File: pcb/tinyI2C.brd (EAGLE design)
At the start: 83.2 x 83.2 mm, 34 parts, among them IC1 74LVC1G125DCK, IC2 74LVC1G125DCK, IC3 IC_LDO_MIC5355, U1 LPC824M201JHI33, X1 TSW-112-02-S-S, X2 TSW-112-02-S-S, X3 TSW-106-02-S-S-RA, X4 TSW-102-02-S-S, X5 TSW-102-02-S-S, X6 TSW-102-02-S-S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

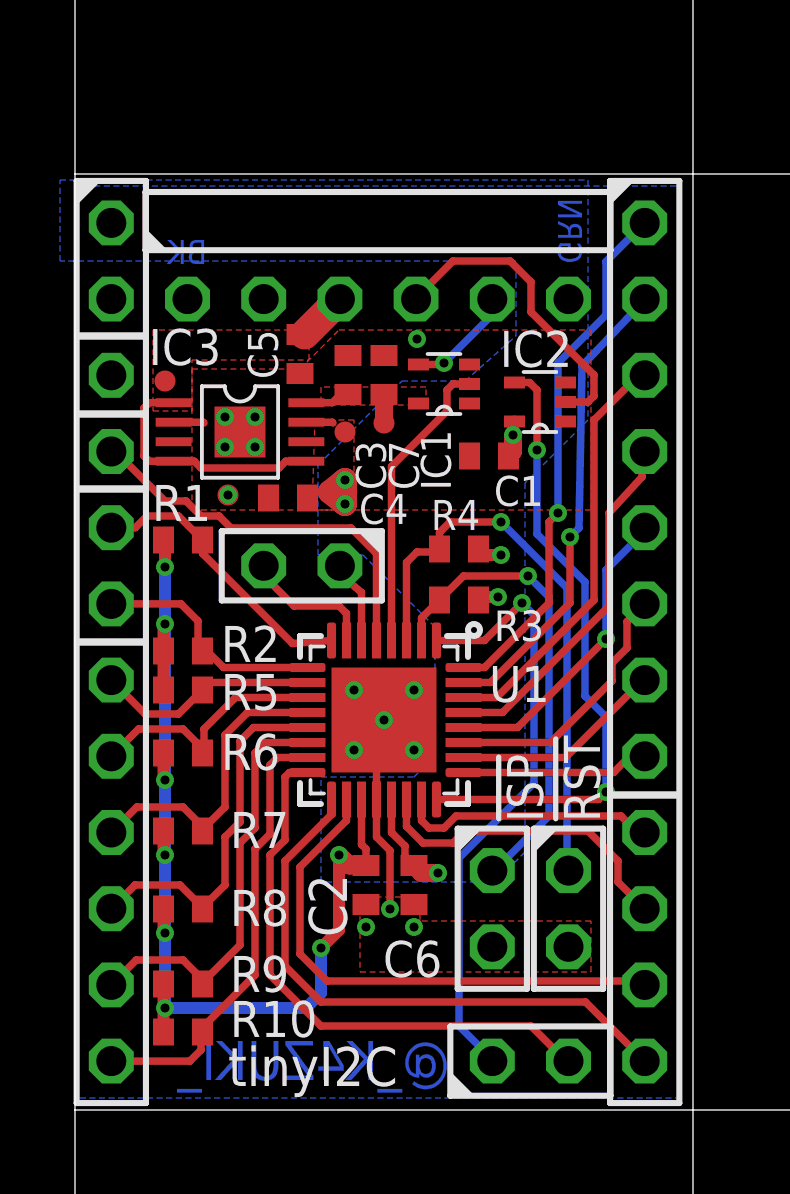
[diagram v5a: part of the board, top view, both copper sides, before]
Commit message: [ PCB ][ SCH ] X1[3] is now Vin(5V) [ BRD ] related tracechange
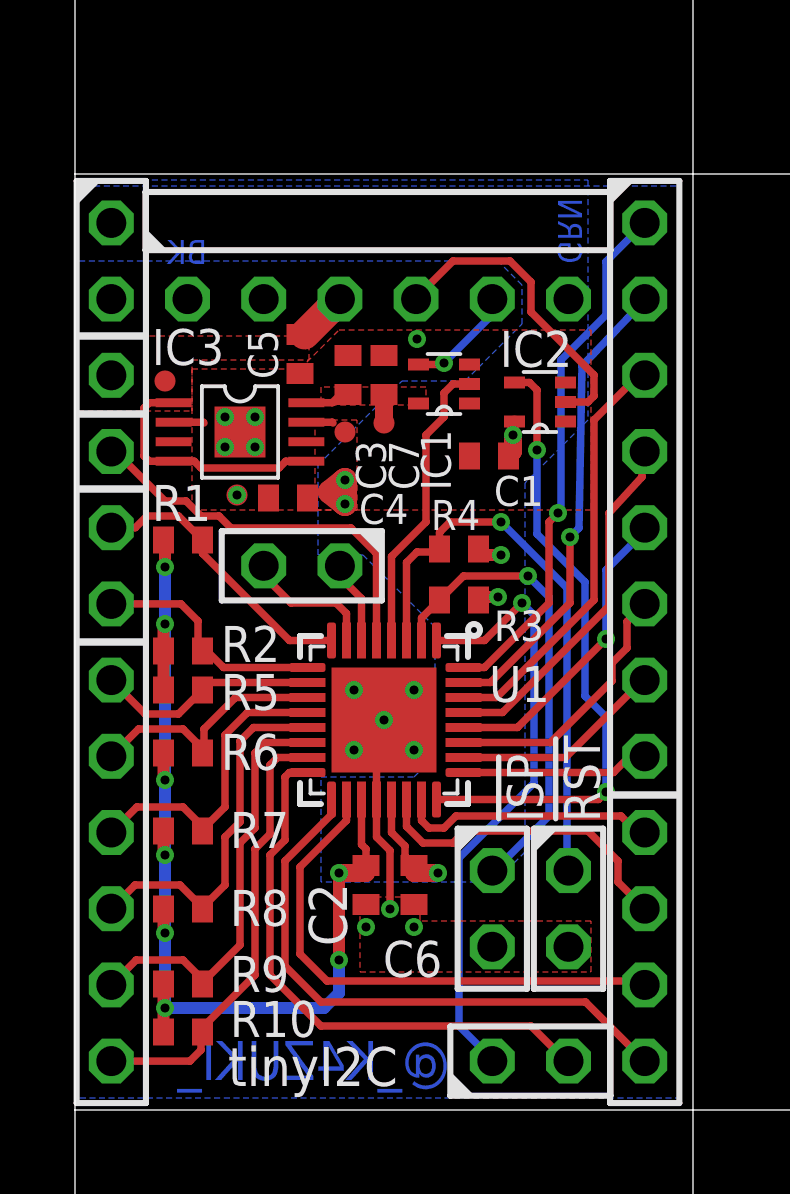
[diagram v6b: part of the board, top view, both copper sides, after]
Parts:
- moved TP3 0.30 mm to (5.40, 30.9)
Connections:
- net 5V: now also X1.3
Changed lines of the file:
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@@
 <text x="17.5" y="20" size="1.2" layer="21" font="vector" ratio="15" rot="R90">!RST</text>
 <text x="15.6" y="20" size="1.2" layer="21" font="vector" ratio="15" rot="R90">!ISP</text>
+<wire x1="6.8" y1="30.3" x2="6.8" y2="31.3" width="0.2" layer="41"/>
+<wire x1="6.8" y1="30.3" x2="6.1" y2="30.3" width="0.2" layer="41"/>
+<wire x1="6.8" y1="31.3" x2="6.1" y2="31.3" width="0.2" layer="41"/>
+<wire x1="0.2" y1="11" x2="0.2" y2="41" width="0.4" layer="41"/>
+<wire x1="20.1" y1="41" x2="0.2" y2="41" width="0.4" layer="41"/>
+<wire x1="20.1" y1="41" x2="20.1" y2="11" width="0.4" layer="41"/>
+<wire x1="0.2" y1="11" x2="20.1" y2="11" width="0.4" layer="41"/>
 </plain>
 <attributes>
@@
 </element>
 <element name="C2" library="mylib" package="C0402" value="1005" x="9.7" y="17.9" smashed="yes" rot="R270">
-<attribute name="NAME" x="9.065" y="16.165" size="1.27" layer="25" font="vector" ratio="15" rot="R90"/>
+<attribute name="NAME" x="9.065" y="15.865" size="1.27" layer="25" font="vector" ratio="15" rot="R90"/>
 <attribute name="VALUE" x="7.795" y="18.535" size="1.27" layer="27" rot="R270"/>
 </element>
@@
 <attribute name="VALUE" x="8.746" y="32.492" size="0.0254" layer="27"/>
 </element>
-<element name="TP3" library="testpad" package="TP07R" value="TPTP07R" x="5.1" y="30.9" smashed="yes">
-<attribute name="TP_SIGNAL_NAME" value="" x="5.1" y="28.995" size="1" layer="37"/>
-<attribute name="VALUE" x="4.846" y="30.392" size="0.0254" layer="27"/>
+<element name="TP3" library="testpad" package="TP07R" value="TPTP07R" x="5.4" y="30.9" smashed="yes">
+<attribute name="TP_SIGNAL_NAME" value="" x="5.4" y="28.995" size="1" layer="37"/>
+<attribute name="VALUE" x="5.146" y="30.392" size="0.0254" layer="27"/>
 </element>
 <element name="R1" library="mylib" package="C0402" value="220/1005" x="3.6" y="29.4" smashed="yes" rot="R180">
@@
 </element>
 <element name="IC3" library="mylib" package="IC_08_0.65_160MIL" value="IC_LDO_MIC5355" x="5.5" y="33" smashed="yes" rot="R270">
-<attribute name="NAME" x="2.46" y="35.232" size="1.2" layer="25" font="vector" ratio="15"/>
+<attribute name="NAME" x="2.56" y="35.232" size="1.2" layer="25" font="vector" ratio="15"/>
 <attribute name="VALUE" x="2.96" y="29.698" size="1.27" layer="27" ratio="10"/>
 </element>
@@
 </polygon>
 <via x="5" y="32.5" extent="1-16" drill="0.3"/>
-<via x="5.1" y="30.9" extent="1-16" drill="0.3"/>
+<via x="5.4" y="30.9" extent="1-16" drill="0.3"/>
 <via x="6" y="32.5" extent="1-16" drill="0.3"/>
 <polygon width="0.25" layer="1" thermals="no" rank="2">
@@
 <wire x1="6.8" y1="31.8" x2="4.2" y2="31.8" width="0.25" layer="1"/>
 <polygon width="0.25" layer="1" thermals="no" rank="3">
-<vertex x="2.6" y="33.7"/>
+<vertex x="0.1" y="33.7"/>
 <vertex x="3.9" y="33.7"/>
 <vertex x="3.9" y="35.4"/>
 <vertex x="7.8" y="35.4"/>
-<vertex x="7.8" y="36.4"/>
-<vertex x="2.6" y="36.4"/>
+<vertex x="7.8" y="36.2"/>
+<vertex x="0.1" y="36.2"/>
 </polygon>
 <wire x1="7.65" y1="36.25" x2="8.83" y2="37.43" width="1" layer="1"/>
@@
 <contactref element="IC3" pad="4"/>
 <contactref element="IC3" pad="5"/>
+<contactref element="X1" pad="3"/>
+<wire x1="7.5" y1="36.25" x2="7.65" y2="36.25" width="0.4" layer="1"/>
 </signal>
 <signal name="TX-&gt;">
@@
 <vertex x="10.9" y="34.7"/>
 <vertex x="13" y="34.7"/>
-<vertex x="14.7" y="36.2"/>
-<vertex x="14.7" y="38.7"/>
-<vertex x="-0.5" y="38.7"/>
-<vertex x="-0.5" y="41.4"/>
+<vertex x="14.9" y="36.6"/>
+<vertex x="14.9" y="37.9"/>
+<vertex x="14.1" y="38.7"/>
+<vertex x="0" y="38.7"/>
+<vertex x="0" y="41.4"/>
 <vertex x="17.1" y="41.4"/>
 <vertex x="17.1" y="33.4"/>
@@
 <contactref element="C6" pad="1"/>
 <wire x1="10.55" y1="19.65" x2="11" y2="19.2" width="0.25" layer="1"/>
-<via x="8.8" y="18.9" extent="1-16" drill="0.3"/>
+<via x="8.8" y="18.3" extent="1-16" drill="0.3"/>
 <wire x1="11" y1="19.2" x2="11" y2="18.85" width="0.25" layer="1"/>
-<wire x1="12.1" y1="18.3" x2="11.55" y2="18.3" width="0.6" layer="1"/>
+<wire x1="12.1" y1="18.3" x2="11.3" y2="18.3" width="0.6" layer="1"/>
 <wire x1="3" y1="18.9" x2="3" y2="21.4" width="0.4" layer="16"/>
 <wire x1="3" y1="16.3" x2="3" y2="18.9" width="0.4" layer="16"/>
 <wire x1="3" y1="13.8" x2="3" y2="16.3" width="0.4" layer="16"/>
-<via x="8.2" y="15.8" extent="1-16" drill="0.3" diameter="0.6"/>
+<via x="8.8" y="15.4" extent="1-16" drill="0.3" diameter="0.6"/>
 <wire x1="11" y1="18.85" x2="11.3" y2="18.55" width="0.25" layer="1"/>
-<wire x1="11.55" y1="18.3" x2="11.3" y2="18.55" width="0.6" layer="1"/>
-<wire x1="9.7" y1="18.55" x2="9.15" y2="18.55" width="0.6" layer="1"/>
-<wire x1="9.15" y1="18.55" x2="8.8" y2="18.9" width="0.6" layer="1"/>
 <wire x1="9.55" y1="20.75" x2="9.55" y2="19.25" width="0.25" layer="1"/>
 <wire x1="9.7" y1="18.55" x2="9.7" y2="19.1" width="0.25" layer="1"/>
@@
 <wire x1="2.95" y1="13" x2="2.95" y2="13.75" width="0.4" layer="1"/>
 <wire x1="2.95" y1="13.75" x2="3" y2="13.8" width="0.4" layer="1"/>
-<wire x1="8.8" y1="18.9" x2="8.8" y2="16.4" width="0.4" layer="1"/>
-<wire x1="8.2" y1="15.8" x2="8.2" y2="14.3" width="0.4" layer="16"/>
-<wire x1="8.2" y1="15.8" x2="8.8" y2="16.4" width="0.4" layer="1"/>
-<wire x1="3" y1="13.8" x2="7.7" y2="13.8" width="0.4" layer="16"/>
-<wire x1="7.7" y1="13.8" x2="8.2" y2="14.3" width="0.4" layer="16"/>
+<wire x1="8.8" y1="18.3" x2="8.8" y2="15.4" width="0.4" layer="1"/>
+<wire x1="8.8" y1="15.4" x2="8.8" y2="14.3" width="0.4" layer="16"/>
+<wire x1="3" y1="13.8" x2="8.3" y2="13.8" width="0.4" layer="16"/>
+<wire x1="8.3" y1="13.8" x2="8.8" y2="14.3" width="0.4" layer="16"/>
 <wire x1="7.712" y1="33.326" x2="8.574" y2="33.326" width="0.25" layer="1"/>
 <wire x1="8.574" y1="33.326" x2="8.6" y2="33.3" width="0.25" layer="1"/>
 <contactref element="IC2" pad="5"/>
 <polygon width="0.25" layer="1" thermals="no">
-<vertex x="9.3" y="33.4"/>
+<vertex x="9.4" y="33.4"/>
 <vertex x="8" y="33.4"/>
-<vertex x="7.9" y="30.4"/>
-<vertex x="9.3" y="30.4"/>
+<vertex x="8" y="30.4"/>
+<vertex x="9.4" y="30.4"/>
 </polygon>
 <contactref element="IC3" pad="7"/>
@@
 <wire x1="14.6" y1="32.9" x2="14.6" y2="32.35" width="0.6" layer="1"/>
 <wire x1="14.6" y1="32.35" x2="14.45" y2="32.2" width="0.6" layer="1"/>
+<wire x1="8.8" y1="18.3" x2="9.7" y2="18.3" width="0.6" layer="1"/>
+<wire x1="9.7" y1="18.3" x2="9.7" y2="18.55" width="0.6" layer="1"/>
+<wire x1="11.3" y1="18.3" x2="11.3" y2="18.55" width="0.6" layer="1"/>
 </signal>
 <signal name="TGT_TX">
 <contactref element="U1" pad="4"/>
-<wire x1="10.55" y1="26.05" x2="10.55" y2="31.85" width="0.25" layer="1"/>
+<wire x1="10.55" y1="26.05" x2="10.55" y2="28.85" width="0.25" layer="1"/>
 <contactref element="IC1" pad="2"/>
-<wire x1="10.55" y1="31.85" x2="12.4" y2="33.7" width="0.25" layer="1"/>
+<wire x1="10.55" y1="28.85" x2="11.7" y2="30" width="0.25" layer="1"/>
 <wire x1="13.15" y1="34.6" x2="12.6" y2="34.6" width="0.25" layer="1"/>
-<wire x1="12.6" y1="34.6" x2="12.4" y2="34.4" width="0.25" layer="1"/>
-<wire x1="12.4" y1="34.4" x2="12.4" y2="33.7" width="0.25" layer="1"/>
+<wire x1="12.6" y1="34.6" x2="12.3" y2="34.3" width="0.25" layer="1"/>
+<wire x1="12.3" y1="34.3" x2="12.3" y2="33.5" width="0.25" layer="1"/>
+<wire x1="12.3" y1="33.5" x2="11.7" y2="32.9" width="0.25" layer="1"/>
+<wire x1="11.7" y1="32.9" x2="11.7" y2="30" width="0.25" layer="1"/>
 </signal>
 <signal name="TGT_RX">
@@
 <signal name="SWCLK">
 <contactref element="U1" pad="6"/>
-<wire x1="9.55" y1="26.05" x2="9.55" y2="27.65" width="0.25" layer="1"/>
+<wire x1="9.55" y1="26.05" x2="9.55" y2="27.45" width="0.25" layer="1"/>
 <contactref element="X5" pad="1"/>
-<wire x1="8.83" y1="28.54" x2="8.83" y2="28.27" width="0.25" layer="1"/>
-<wire x1="8.83" y1="28.27" x2="9.55" y2="27.65" width="0.25" layer="1"/>
+<wire x1="8.83" y1="28.54" x2="8.83" y2="28.17" width="0.25" layer="1"/>
+<wire x1="8.83" y1="28.17" x2="9.55" y2="27.45" width="0.25" layer="1"/>
 </signal>
 <signal name="SWDIO">
 <contactref element="U1" pad="7"/>
 <wire x1="9.05" y1="26.05" x2="9.05" y2="26.95" width="0.25" layer="1"/>
-<wire x1="9.05" y1="26.95" x2="8.8" y2="27.2" width="0.25" layer="1"/>
-<wire x1="8.8" y1="27.2" x2="7.3" y2="27.2" width="0.25" layer="1"/>
+<wire x1="9.05" y1="26.95" x2="8.7" y2="27.3" width="0.25" layer="1"/>
+<wire x1="8.7" y1="27.3" x2="7.2" y2="27.3" width="0.25" layer="1"/>
 <contactref element="X5" pad="2"/>
-<wire x1="6.29" y1="28.21" x2="7.3" y2="27.2" width="0.25" layer="1"/>
+<wire x1="6.29" y1="28.21" x2="7.2" y2="27.3" width="0.25" layer="1"/>
 <wire x1="6.29" y1="28.54" x2="6.29" y2="28.21" width="0.25" layer="1"/>
 </signal>
@@
 <contactref element="R1" pad="1"/>
 <contactref element="X1" pad="5"/>
-<wire x1="8.55" y1="26.05" x2="7.25" y2="25.95" width="0.25" layer="1"/>
+<wire x1="8.55" y1="26.05" x2="7.15" y2="26.05" width="0.25" layer="1"/>
 <wire x1="1.21" y1="29.81" x2="2.01" y2="29.81" width="0.25" layer="1"/>
 <wire x1="2.01" y1="29.81" x2="2.4" y2="30.2" width="0.25" layer="1"/>
@@
 <wire x1="3.45" y1="30.2" x2="4.25" y2="29.4" width="0.25" layer="1"/>
 <wire x1="4.25" y1="29.4" x2="4.25" y2="28.95" width="0.25" layer="1"/>
-<wire x1="4.25" y1="28.95" x2="7.25" y2="25.95" width="0.25" layer="1"/>
+<wire x1="4.25" y1="28.95" x2="7.15" y2="26.05" width="0.25" layer="1"/>
 </signal>
 <signal name="I2C_SCL">
@@
 <wire x1="15.8" y1="27.3" x2="15.8" y2="30" width="0.25" layer="1"/>
 <wire x1="15.8" y1="30" x2="16.1" y2="30.3" width="0.25" layer="1"/>
-<wire x1="16.1" y1="30.3" x2="16.1" y2="35.3" width="0.25" layer="16"/>
-<wire x1="16.1" y1="35.3" x2="17.7" y2="36.9" width="0.25" layer="16"/>
+<wire x1="16.1" y1="30.3" x2="16.2" y2="30.4" width="0.25" layer="16"/>
+<wire x1="16.2" y1="30.4" x2="16.2" y2="35.4" width="0.25" layer="16"/>
+<wire x1="16.2" y1="35.4" x2="17.7" y2="36.9" width="0.25" layer="16"/>
 <wire x1="18.99" y1="39.97" x2="17.7" y2="38.68" width="0.25" layer="16"/>
 <wire x1="17.7" y1="38.68" x2="17.7" y2="36.9" width="0.25" layer="16"/>

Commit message: .
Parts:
- moved R1 0.40 mm to (3.60, 29.0)
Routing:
- net I2C_SDA: track 9.48 -> 8.93 mm
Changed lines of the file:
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@@
 <wire x1="20.1" y1="41" x2="20.1" y2="11" width="0.4" layer="41"/>
 <wire x1="0.2" y1="11" x2="20.1" y2="11" width="0.4" layer="41"/>
+<wire x1="2.3" y1="20.9" x2="0.1" y2="20.9" width="0.25" layer="21"/>
+<wire x1="2.3" y1="15.8" x2="0.1" y2="15.8" width="0.25" layer="21"/>
+<polygon width="0.25" layer="21">
+<vertex x="1.2" y="27.3"/>
+<vertex x="2.3" y="28.4"/>
+<vertex x="2.3" y="26.2"/>
+</polygon>
+<polygon width="0.25" layer="21">
+<vertex x="1.2" y="22.2"/>
+<vertex x="2.3" y="23.3"/>
+<vertex x="2.3" y="21.1"/>
+</polygon>
+<polygon width="0.25" layer="21">
+<vertex x="1.2" y="17.1"/>
+<vertex x="2.3" y="18.2"/>
+<vertex x="2.3" y="16"/>
+</polygon>
+<polygon width="0.25" layer="21">
+<vertex x="1.2" y="12"/>
+<vertex x="2.3" y="13.1"/>
+<vertex x="2.3" y="10.9"/>
+</polygon>
+<polygon width="0.25" layer="21">
+<vertex x="19" y="14.6"/>
+<vertex x="17.9" y="13.5"/>
+<vertex x="17.9" y="15.7"/>
+</polygon>
+<polygon width="0.25" layer="21">
+<vertex x="20.2" y="19.7"/>
+<vertex x="19" y="18.5"/>
+<vertex x="19" y="20.9"/>
+</polygon>
+<polygon width="0.25" layer="21">
+<vertex x="17.8" y="17.1"/>
+<vertex x="19" y="18.3"/>
+<vertex x="19" y="15.9"/>
+</polygon>
 </plain>
 <attributes>
@@
 <attribute name="VALUE" x="5.146" y="30.392" size="0.0254" layer="27"/>
 </element>
-<element name="R1" library="mylib" package="C0402" value="220/1005" x="3.6" y="29.4" smashed="yes" rot="R180">
-<attribute name="NAME" x="2.565" y="30.035" size="1.2" layer="25" font="vector" ratio="15"/>
-<attribute name="VALUE" x="4.235" y="31.305" size="1.27" layer="27" rot="R180"/>
+<element name="R1" library="mylib" package="C0402" value="220/1005" x="3.6" y="29" smashed="yes" rot="R180">
+<attribute name="NAME" x="2.565" y="29.635" size="1.2" layer="25" font="vector" ratio="15"/>
+<attribute name="VALUE" x="4.235" y="30.905" size="1.27" layer="27" rot="R180"/>
 </element>
 <element name="R2" library="mylib" package="C0402" value="220/1005" x="3.6" y="25.7" smashed="yes" rot="R180">
@@
 <contactref element="C5" pad="1"/>
 <contactref element="TP1" pad="TP"/>
-<wire x1="3.287" y1="32.026" x2="2.474" y2="32.026" width="0.25" layer="1"/>
-<wire x1="2.474" y1="32.026" x2="2.3" y2="32.2" width="0.25" layer="1"/>
-<wire x1="3.287" y1="33.976" x2="2.476" y2="33.976" width="0.25" layer="1"/>
-<wire x1="2.476" y1="33.976" x2="2.3" y2="33.8" width="0.25" layer="1"/>
-<wire x1="2.3" y1="33.8" x2="2.3" y2="32.2" width="0.25" layer="1"/>
+<wire x1="3.287" y1="32.026" x2="2.574" y2="32.026" width="0.25" layer="1"/>
+<wire x1="2.574" y1="32.026" x2="2.3" y2="32.3" width="0.25" layer="1"/>
+<wire x1="3.287" y1="33.976" x2="2.576" y2="33.976" width="0.25" layer="1"/>
+<wire x1="2.576" y1="33.976" x2="2.3" y2="33.7" width="0.25" layer="1"/>
+<wire x1="2.3" y1="33.7" x2="2.3" y2="32.3" width="0.25" layer="1"/>
 <wire x1="3.287" y1="32.026" x2="3.974" y2="32.026" width="0.25" layer="1"/>
 <wire x1="3.974" y1="32.026" x2="4.2" y2="31.8" width="0.25" layer="1"/>
@@
 <via x="3" y="26.6" extent="1-16" drill="0.3" diameter="0.6"/>
 <wire x1="3" y1="21.4" x2="3" y2="26.6" width="0.4" layer="16"/>
-<via x="3" y="28.5" extent="1-16" drill="0.3" diameter="0.6"/>
-<wire x1="3" y1="26.6" x2="3" y2="28.5" width="0.4" layer="16"/>
+<via x="3" y="28" extent="1-16" drill="0.3" diameter="0.6"/>
+<wire x1="3" y1="26.6" x2="3" y2="28" width="0.4" layer="16"/>
 <wire x1="2.95" y1="24.4" x2="2.95" y2="25.7" width="0.4" layer="1"/>
-<wire x1="3" y1="28.5" x2="3" y2="29.35" width="0.4" layer="1"/>
-<wire x1="3" y1="29.35" x2="2.95" y2="29.4" width="0.4" layer="1"/>
+<wire x1="3" y1="28" x2="3" y2="28.95" width="0.4" layer="1"/>
+<wire x1="3" y1="28.95" x2="2.95" y2="29" width="0.4" layer="1"/>
 <wire x1="2.95" y1="25.7" x2="2.95" y2="26.55" width="0.4" layer="1"/>
 <wire x1="2.95" y1="26.55" x2="3" y2="26.6" width="0.4" layer="1"/>
@@
 <wire x1="9.2" y1="29.8" x2="10.05" y2="28.95" width="0.25" layer="1"/>
 <wire x1="10.05" y1="26.05" x2="10.05" y2="28.95" width="0.25" layer="1"/>
-<wire x1="5.2" y1="29.8" x2="9.2" y2="29.8" width="0.25" layer="1"/>
+<wire x1="4.6" y1="29.8" x2="9.2" y2="29.8" width="0.25" layer="1"/>
 <wire x1="3" y1="30.7" x2="3.7" y2="30.7" width="0.25" layer="1"/>
-<wire x1="3.7" y1="30.7" x2="4.2" y2="30.2" width="0.25" layer="1"/>
-<wire x1="5.2" y1="29.8" x2="4.8" y2="30.2" width="0.25" layer="1"/>
-<wire x1="4.8" y1="30.2" x2="4.2" y2="30.2" width="0.25" layer="1"/>
+<wire x1="3.7" y1="30.7" x2="4.6" y2="29.8" width="0.25" layer="1"/>
 </signal>
 <signal name="SWCLK">
@@
 <contactref element="X1" pad="5"/>
 <wire x1="8.55" y1="26.05" x2="7.15" y2="26.05" width="0.25" layer="1"/>
-<wire x1="1.21" y1="29.81" x2="2.01" y2="29.81" width="0.25" layer="1"/>
-<wire x1="2.01" y1="29.81" x2="2.4" y2="30.2" width="0.25" layer="1"/>
-<wire x1="2.4" y1="30.2" x2="3.45" y2="30.2" width="0.25" layer="1"/>
-<wire x1="3.45" y1="30.2" x2="4.25" y2="29.4" width="0.25" layer="1"/>
-<wire x1="4.25" y1="29.4" x2="4.25" y2="28.95" width="0.25" layer="1"/>
+<wire x1="1.21" y1="29.8" x2="3.45" y2="29.8" width="0.25" layer="1"/>
+<wire x1="3.45" y1="29.8" x2="4.25" y2="29" width="0.25" layer="1"/>
+<wire x1="4.25" y1="29" x2="4.25" y2="28.95" width="0.25" layer="1"/>
 <wire x1="4.25" y1="28.95" x2="7.15" y2="26.05" width="0.25" layer="1"/>
+<wire x1="1.21" y1="29.8" x2="1.21" y2="29.81" width="0.25" layer="1"/>
 </signal>
 <signal name="I2C_SCL">
